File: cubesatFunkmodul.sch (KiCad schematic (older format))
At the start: 0 parts

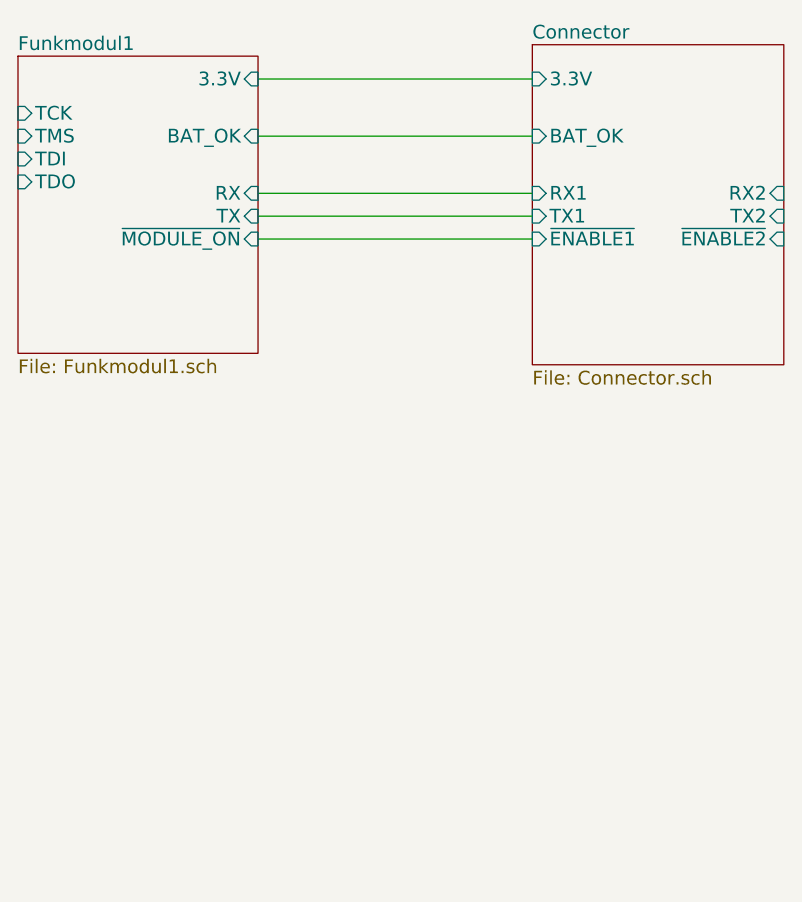
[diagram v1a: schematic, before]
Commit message: Integrates Connectors in Design
Beginn to add mounting holes
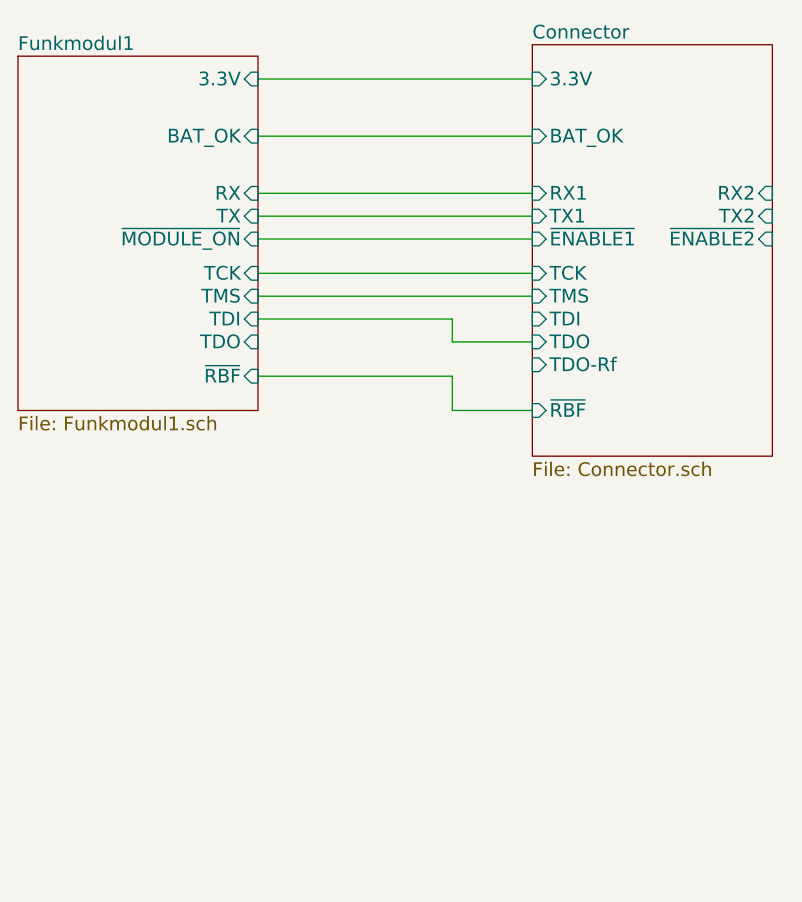
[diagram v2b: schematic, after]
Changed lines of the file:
@@
 LIBS:nxp-ic
 LIBS:7400-ic
-LIBS:cubesatFunkmodul-cache
 LIBS:funkmodul
 LIBS:CubeSat-Bus-1
 LIBS:CubeSat-Bus-2
+LIBS:disco-con
 EELAYER 25 0
 EELAYER END
@@
 $EndDescr
 $Sheet
-S 2650 2450 1050 1300
+S 2650 2450 1050 1550
 U 5993797A
 F0 "Funkmodul1" 60
@@
 F4 "3.3V" I R 3700 2550 60
 F5 "~MODULE_ON~" I R 3700 3250 60
-F6 "TCK" I L 2650 2700 60
-F7 "TMS" I L 2650 2800 60
-F8 "TDO" I L 2650 3000 60
-F9 "TDI" I L 2650 2900 60
+F6 "TCK" I R 3700 3400 60
+F7 "TMS" I R 3700 3500 60
+F8 "TDO" I R 3700 3700 60
+F9 "TDI" I R 3700 3600 60
 F10 "BAT_OK" I R 3700 2800 60
+F11 "~RBF~" I R 3700 3850 60
 $EndSheet
 $Sheet
-S 4900 2400 1100 1400
+S 4900 2400 1050 1800
 U 59C45183
 F0 "Connector" 60
@@
 F3 "TX1" I L 4900 3150 60
 F4 "~ENABLE1~" I L 4900 3250 60
-F5 "RX2" I R 6000 3050 60
-F6 "TX2" I R 6000 3150 60
-F7 "~ENABLE2~" I R 6000 3250 60
+F5 "RX2" I R 5950 3050 60
+F6 "TX2" I R 5950 3150 60
+F7 "~ENABLE2~" I R 5950 3250 60
 F8 "3.3V" I L 4900 2550 60
 F9 "BAT_OK" I L 4900 2800 60
+F10 "TCK" I L 4900 3400 60
+F11 "TMS" I L 4900 3500 60
+F12 "TDI" I L 4900 3600 60
+F13 "TDO" I L 4900 3700 60
+F14 "TDO-Rf" I L 4900 3800 60
+F15 "~RBF~" I L 4900 4000 60
 $EndSheet
 Wire Wire Line
@@
 Wire Wire Line
 	3700 2800 4900 2800
+Wire Wire Line
+	4900 3700 4550 3700
+Wire Wire Line
+	4550 3700 4550 3600
+Wire Wire Line
+	4550 3600 3700 3600
+Wire Wire Line
+	4900 3500 3700 3500
+Wire Wire Line
+	4900 3400 3700 3400
+Wire Wire Line
+	3700 3850 4550 3850
+Wire Wire Line
+	4550 3850 4550 4000
+Wire Wire Line
+	4550 4000 4900 4000
 $EndSCHEMATC

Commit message: Adds new unit
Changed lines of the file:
@@
 LIBS:nxp-ic
 LIBS:7400-ic
+LIBS:cubesatFunkmodul-cache
 LIBS:funkmodul
 LIBS:CubeSat-Bus-1
@@
 $Descr A4 11693 8268
 encoding utf-8
-Sheet 1 4
+Sheet 1 6
 Title ""
 Date ""
@@
 Wire Wire Line
 	4550 4000 4900 4000
+$Sheet
+S 2650 4250 1050 1550
+U 59FF6F05
+F0 "Funkmodul2" 60
+F1 "Funkmodul2.sch" 60
+F2 "RX" I R 3700 4850 60
+F3 "TX" I R 3700 4950 60
+F4 "3.3V" I R 3700 4350 60
+F5 "~MODULE_ON~" I R 3700 5050 60
+F6 "TCK" I R 3700 5200 60
+F7 "TMS" I R 3700 5300 60
+F8 "TDO" I R 3700 5500 60
+F9 "TDI" I R 3700 5400 60
+F10 "BAT_OK" I R 3700 4600 60
+F11 "~RBF~" I R 3700 5650 60
+$EndSheet
 $EndSCHEMATC

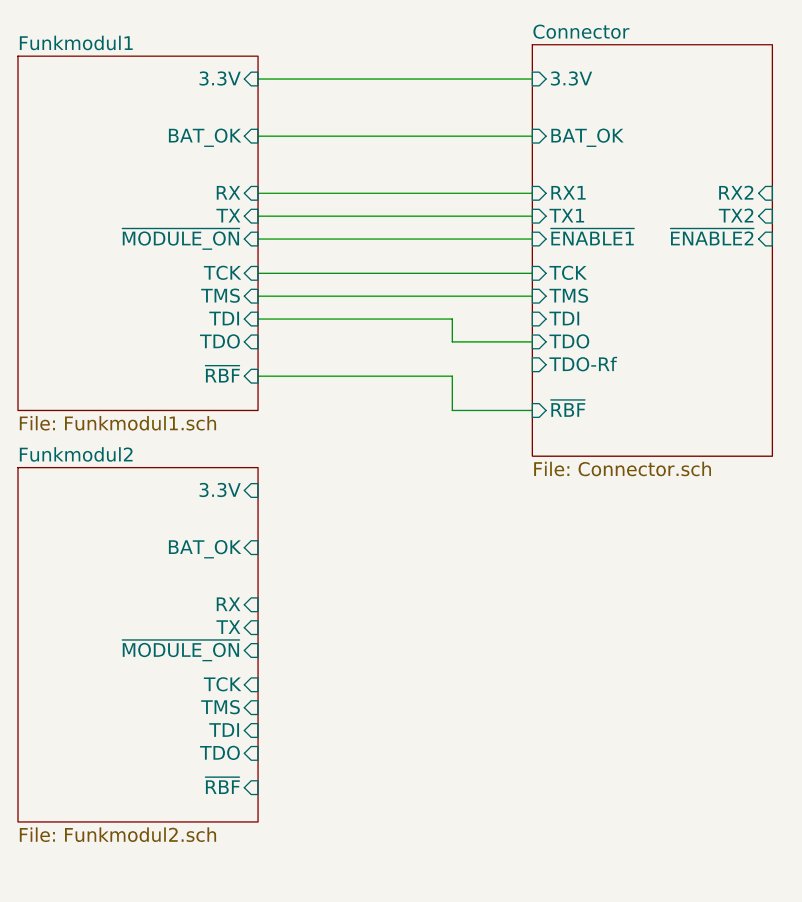
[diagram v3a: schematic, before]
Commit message: Places all Components of second module
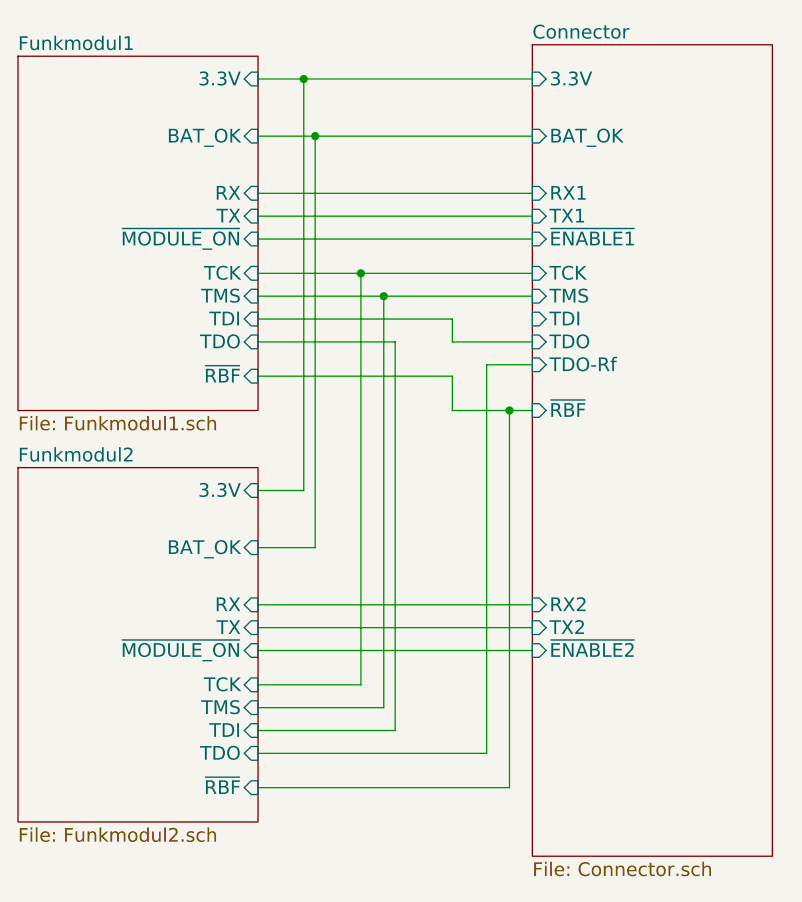
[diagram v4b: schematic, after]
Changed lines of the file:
@@
 $EndSheet
 $Sheet
-S 4900 2400 1050 1800
+S 4900 2400 1050 3550
 U 59C45183
 F0 "Connector" 60
@@
 F3 "TX1" I L 4900 3150 60
 F4 "~ENABLE1~" I L 4900 3250 60
-F5 "RX2" I R 5950 3050 60
-F6 "TX2" I R 5950 3150 60
-F7 "~ENABLE2~" I R 5950 3250 60
+F5 "RX2" I L 4900 4850 60
+F6 "TX2" I L 4900 4950 60
+F7 "~ENABLE2~" I L 4900 5050 60
 F8 "3.3V" I L 4900 2550 60
 F9 "BAT_OK" I L 4900 2800 60
@@
 F11 "~RBF~" I R 3700 5650 60
 $EndSheet
+Wire Wire Line
+	3700 4350 3900 4350
+Wire Wire Line
+	3900 4350 3900 2550
+Connection ~ 3900 2550
+Wire Wire Line
+	3700 4600 3950 4600
+Wire Wire Line
+	3950 4600 3950 2800
+Connection ~ 3950 2800
+Wire Wire Line
+	3700 4850 4900 4850
+Wire Wire Line
+	3700 4950 4900 4950
+Wire Wire Line
+	3700 5050 4900 5050
+Wire Wire Line
+	3700 5200 4150 5200
+Wire Wire Line
+	4150 5200 4150 3400
+Connection ~ 4150 3400
+Wire Wire Line
+	3700 5300 4250 5300
+Wire Wire Line
+	4250 5300 4250 3500
+Connection ~ 4250 3500
+Wire Wire Line
+	3700 3700 4300 3700
+Wire Wire Line
+	4300 3700 4300 5400
+Wire Wire Line
+	4300 5400 3700 5400
+Wire Wire Line
+	3700 5500 4700 5500
+Wire Wire Line
+	4700 5500 4700 3800
+Wire Wire Line
+	4700 3800 4900 3800
+Wire Wire Line
+	3700 5650 4800 5650
+Wire Wire Line
+	4800 5650 4800 4000
+Connection ~ 4800 4000
 $EndSCHEMATC

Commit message: Adds second burnwire fets
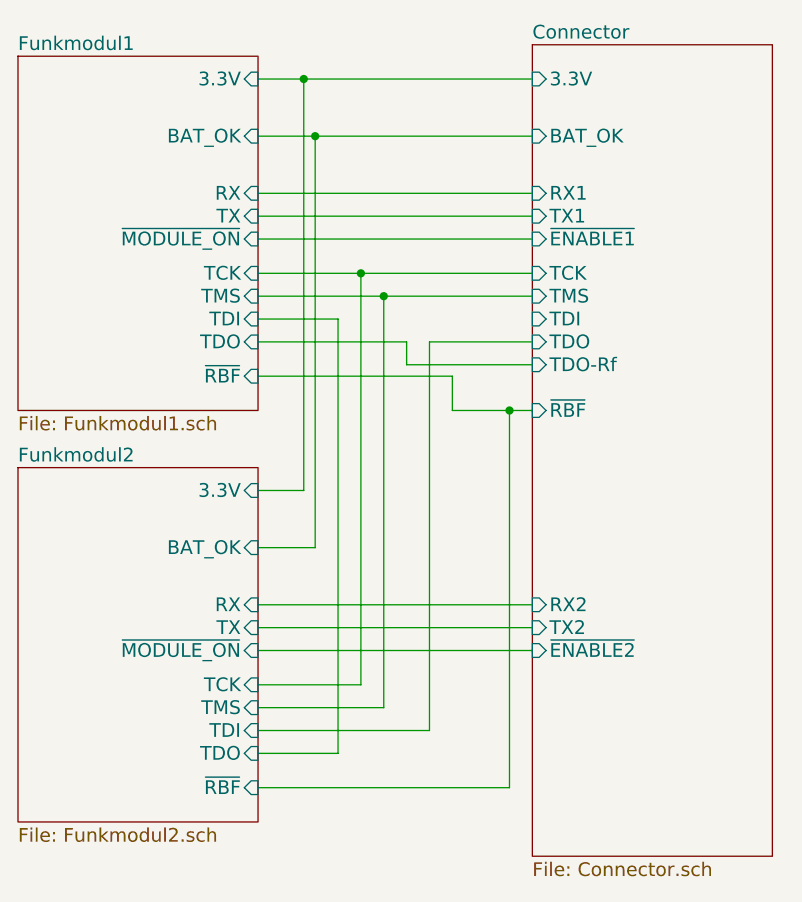
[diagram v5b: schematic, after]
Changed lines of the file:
@@
 	3700 2800 4900 2800
 Wire Wire Line
-	4900 3700 4550 3700
-Wire Wire Line
-	4550 3700 4550 3600
-Wire Wire Line
-	4550 3600 3700 3600
+	4450 3700 4900 3700
 Wire Wire Line
 	4900 3500 3700 3500
@@
 Connection ~ 4250 3500
 Wire Wire Line
-	3700 3700 4300 3700
-Wire Wire Line
-	4300 3700 4300 5400
-Wire Wire Line
-	4300 5400 3700 5400
-Wire Wire Line
-	3700 5500 4700 5500
-Wire Wire Line
-	4700 5500 4700 3800
-Wire Wire Line
-	4700 3800 4900 3800
+	3700 5400 4450 5400
 Wire Wire Line
 	3700 5650 4800 5650
@@
 	4800 5650 4800 4000
 Connection ~ 4800 4000
+Wire Wire Line
+	4450 5400 4450 3700
+Wire Wire Line
+	3700 5500 4050 5500
+Wire Wire Line
+	4050 5500 4050 3600
+Wire Wire Line
+	4050 3600 3700 3600
+Wire Wire Line
+	3700 3700 4350 3700
+Wire Wire Line
+	4350 3700 4350 3800
+Wire Wire Line
+	4350 3800 4900 3800
 $EndSCHEMATC

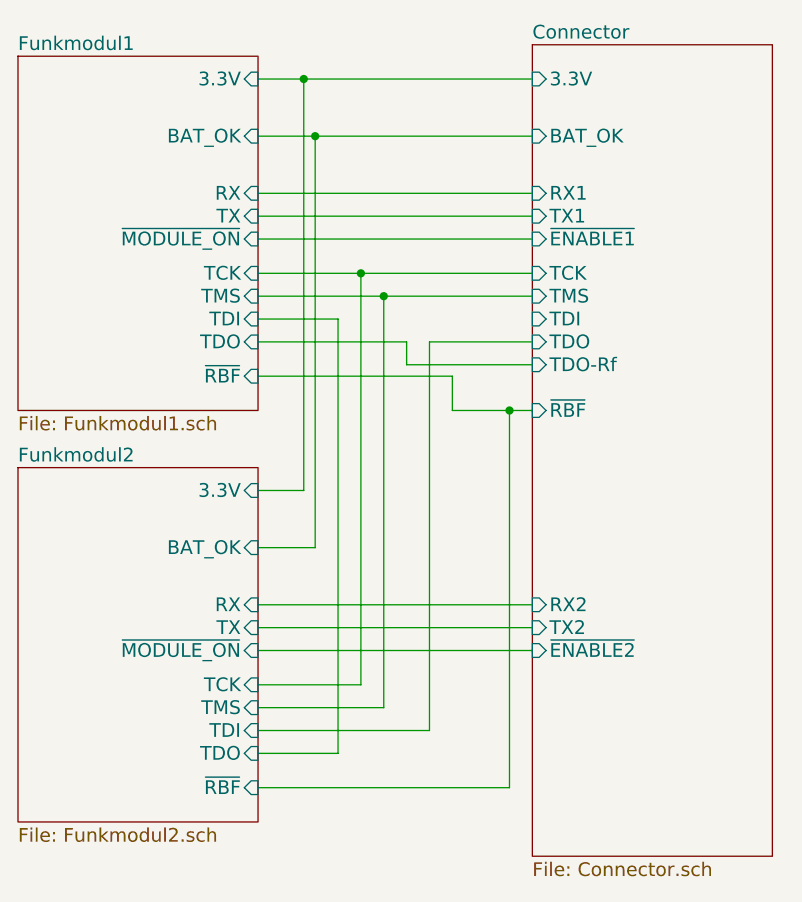
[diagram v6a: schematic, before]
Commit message: Adds stiching vias
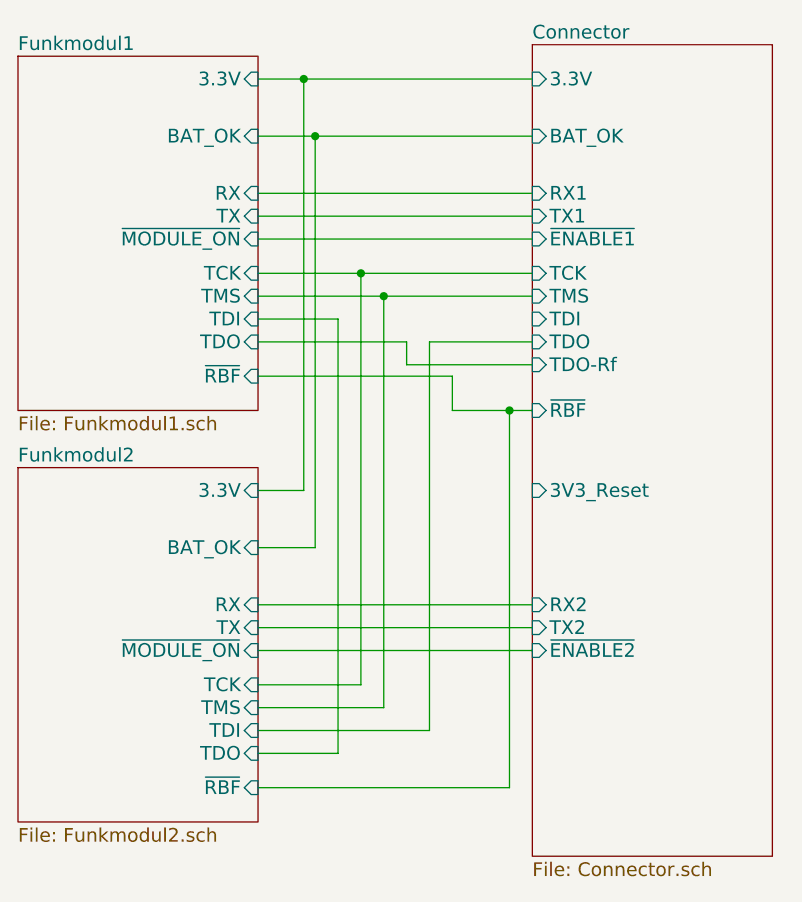
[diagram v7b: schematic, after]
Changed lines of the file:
@@
 LIBS:contrib
 LIBS:valves
+LIBS:nxp-ic
+LIBS:7400-ic
 LIBS:cubesatFunkmodul-cache
 LIBS:funkmodul
+LIBS:CubeSat-Bus-1
+LIBS:CubeSat-Bus-2
 LIBS:disco-con
 EELAYER 25 0
@@
 F14 "TDO-Rf" I L 4900 3800 60
 F15 "~RBF~" I L 4900 4000 60
+F16 "3V3_Reset" I L 4900 4350 60
 $EndSheet
 Wire Wire Line

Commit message: Adds BOM and production files
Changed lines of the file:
@@
 F10 "BAT_OK" I R 3700 2800 60
 F11 "~RBF~" I R 3700 3850 60
+F12 "RESET_3V3" I R 3700 3950 60
 $EndSheet
 $Sheet
@@
 F10 "BAT_OK" I R 3700 4600 60
 F11 "~RBF~" I R 3700 5650 60
+F12 "RESET_3V3" I R 3700 4750 60
 $EndSheet
 Wire Wire Line
@@
 Wire Wire Line
 	4350 3800 4900 3800
+Wire Wire Line
+	3700 3950 4500 3950
+Wire Wire Line
+	4500 3950 4500 4750
+Wire Wire Line
+	4500 4350 4900 4350
+Wire Wire Line
+	4500 4750 3700 4750
+Connection ~ 4500 4350
 $EndSCHEMATC
